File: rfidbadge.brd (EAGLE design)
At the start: 93.7 x 48.2 mm, 49 parts, among them Q1 BSS123, U1 ATMEGA328P_TQFP, U2 CLRC663, Y1 27.12 MHz

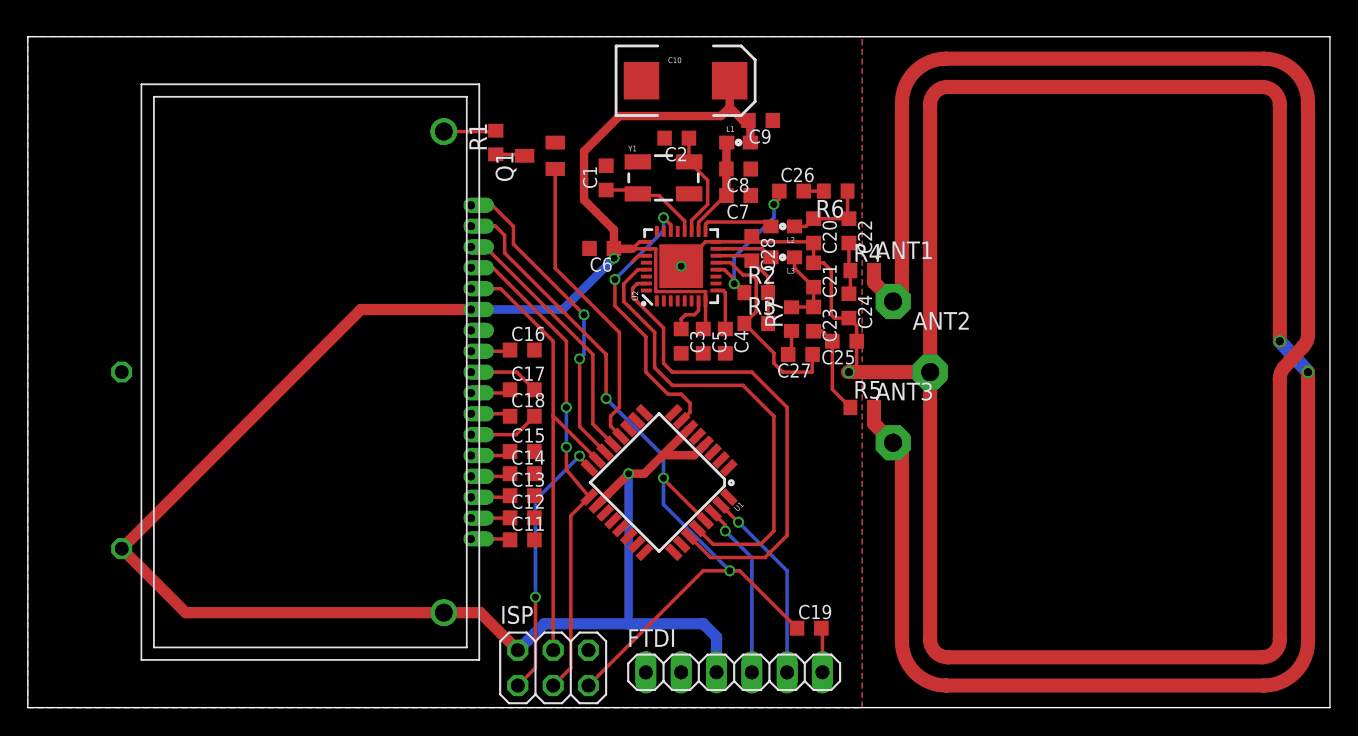
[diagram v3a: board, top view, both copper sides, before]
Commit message: Add switches, lanyard holes, rounded corners
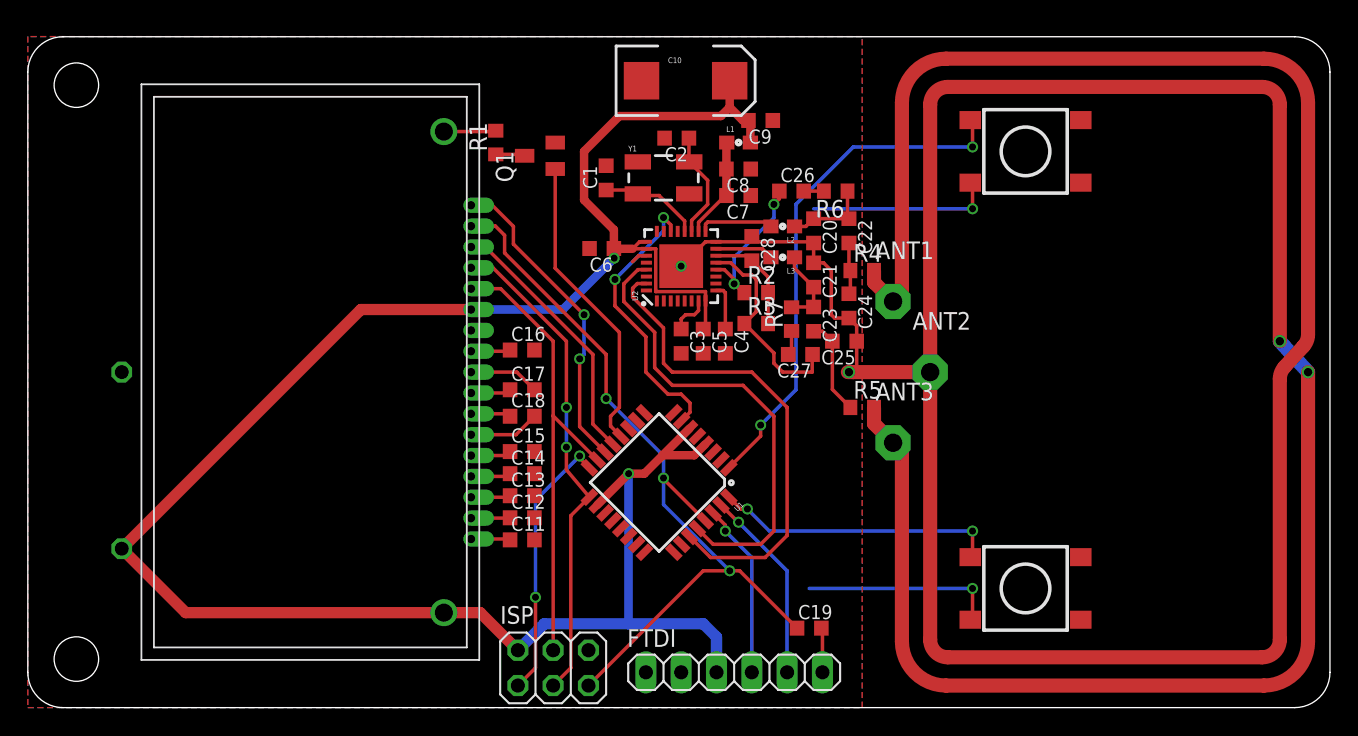
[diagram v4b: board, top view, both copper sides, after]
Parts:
- added S1, S2: SWITCH-MOMENTARY-2SMD-4, SparkFun-Electromechanical:TACTILE_SWITCH_TALL
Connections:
- new net PD2: S1.A2, U1.32
- new net PD3: S2.A2, U1.1
- net GND: now also S1.B2, S2.B2
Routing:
- net PD3: track 0.00 -> 37.5 mm, vias 0 -> 2
- net GND: track 298.4 -> 326.1 mm, vias 4 -> 6
- net PD2: track 0.00 -> 20.6 mm, vias 0 -> 2
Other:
- outline, holes or cut-outs redrawn
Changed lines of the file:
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@@
 <layer number="43" name="vRestrict" color="2" fill="10" visible="yes" active="yes"/>
 <layer number="44" name="Drills" color="7" fill="1" visible="no" active="yes"/>
-<layer number="45" name="Holes" color="7" fill="1" visible="no" active="yes"/>
+<layer number="45" name="Holes" color="7" fill="1" visible="yes" active="yes"/>
 <layer number="46" name="Milling" color="3" fill="1" visible="no" active="yes"/>
 <layer number="47" name="Measures" color="7" fill="1" visible="no" active="yes"/>
@@
 <board>
 <plain>
-<wire x1="0" y1="0" x2="93.65" y2="0" width="0" layer="20"/>
-<wire x1="93.65" y1="0" x2="93.65" y2="48.25" width="0" layer="20"/>
-<wire x1="93.65" y1="48.25" x2="0" y2="48.25" width="0" layer="20"/>
-<wire x1="0" y1="48.25" x2="0" y2="0" width="0" layer="20"/>
+<wire x1="91.11" y1="48.25" x2="2.54" y2="48.25" width="0" layer="20"/>
+<wire x1="2.54" y1="48.25" x2="0" y2="45.71" width="0" layer="20" curve="90"/>
+<wire x1="0" y1="45.71" x2="0" y2="2.54" width="0" layer="20"/>
+<wire x1="0" y1="2.54" x2="2.54" y2="0" width="0" layer="20" curve="90"/>
+<wire x1="2.54" y1="0" x2="91.11" y2="0" width="0" layer="20"/>
+<wire x1="91.11" y1="0" x2="93.65" y2="2.54" width="0" layer="20" curve="90"/>
+<wire x1="93.65" y1="2.54" x2="93.65" y2="45.71" width="0" layer="20"/>
+<wire x1="93.65" y1="45.71" x2="91.11" y2="48.25" width="0" layer="20" curve="90"/>
+<hole x="3.4925" y="3.4925" drill="3.2"/>
+<hole x="3.4925" y="44.7675" drill="3.2"/>
 </plain>
 <attributes>
@@
 <attribute name="PROD_ID" value="36-2479-ND" x="30.48" y="24.13" size="1.778" layer="28" rot="MR0" display="off"/>
 </element>
+<element name="S1" library="SparkFun-Electromechanical" package="TACTILE_SWITCH_TALL" value="SWITCH-MOMENTARY-2SMD-4" x="71.755" y="8.5725" rot="R180">
+<attribute name="PROD_ID" value="SWCH-11966" x="71.755" y="8.5725" size="1.778" layer="27" rot="R180" display="off"/>
+</element>
+<element name="S2" library="SparkFun-Electromechanical" package="TACTILE_SWITCH_TALL" value="SWITCH-MOMENTARY-2SMD-4" x="71.755" y="40.005" rot="R180">
+<attribute name="PROD_ID" value="SWCH-11966" x="71.755" y="40.005" size="1.778" layer="27" rot="R180" display="off"/>
+</element>
 </elements>
 <signals>
@@
 <wire x1="44.49" y1="32.5" x2="43.93" y2="32.5" width="0.254" layer="1"/>
 <wire x1="43.93" y1="32.5" x2="43.4975" y2="32.0675" width="0.254" layer="1"/>
-<wire x1="43.4975" y1="32.0675" x2="40.4" y2="33.02" width="0" layer="19" extent="1-16"/>
+<contactref element="S1" pad="B2"/>
+<contactref element="S2" pad="B2"/>
+<wire x1="67.78" y1="6.3225" x2="67.945" y2="6.3225" width="0.254" layer="1"/>
+<wire x1="67.945" y1="6.3225" x2="67.945" y2="8.5725" width="0.254" layer="1"/>
+<via x="67.945" y="8.5725" extent="1-16" drill="0.5"/>
+<wire x1="67.945" y1="8.5725" x2="56.1975" y2="8.5725" width="0.254" layer="16"/>
+<wire x1="67.78" y1="37.755" x2="67.945" y2="37.755" width="0.254" layer="1"/>
+<wire x1="67.945" y1="37.755" x2="67.945" y2="35.8775" width="0.254" layer="1"/>
+<via x="67.945" y="35.8775" extent="1-16" drill="0.5"/>
+<wire x1="67.945" y1="35.8775" x2="56.515" y2="35.8775" width="0.254" layer="16"/>
+<wire x1="48.15498125" y1="19.51066875" x2="48.5775" y2="25.4775" width="0" layer="19" extent="1-1"/>
 </signal>
 <signal name="EXTCLK">
@@
 <wire x1="46.99" y1="27.94" x2="46.99" y2="27.2275" width="0.254" layer="1"/>
 </signal>
+<signal name="PD2">
+<contactref element="U1" pad="32"/>
+<contactref element="S1" pad="A2"/>
+<wire x1="67.78" y1="10.8225" x2="67.945" y2="10.8225" width="0.254" layer="1"/>
+<wire x1="67.945" y1="10.8225" x2="67.945" y2="12.7" width="0.254" layer="1"/>
+<via x="67.945" y="12.7" extent="1-16" drill="0.5"/>
+<wire x1="67.945" y1="12.7" x2="53.34" y2="12.7" width="0.254" layer="16"/>
+<wire x1="53.34" y1="12.7" x2="51.7525" y2="14.2875" width="0.254" layer="16"/>
+<via x="51.7525" y="14.2875" extent="1-16" drill="0.5"/>
+<wire x1="51.7525" y1="14.2875" x2="51.267296875" y2="14.2875" width="0.254" layer="1"/>
+<wire x1="51.267296875" y1="14.2875" x2="50.417725" y2="15.137071875" width="0.254" layer="1"/>
+</signal>
+<signal name="PD3">
+<contactref element="U1" pad="1"/>
+<contactref element="S2" pad="A2"/>
+<wire x1="67.78" y1="42.255" x2="67.945" y2="42.255" width="0.254" layer="1"/>
+<wire x1="67.945" y1="42.255" x2="67.945" y2="40.3225" width="0.254" layer="1"/>
+<via x="67.945" y="40.3225" extent="1-16" drill="0.5"/>
+<wire x1="67.945" y1="40.3225" x2="59.3725" y2="40.3225" width="0.254" layer="16"/>
+<wire x1="59.3725" y1="40.3225" x2="55.245" y2="36.195" width="0.254" layer="16"/>
+<wire x1="55.245" y1="36.195" x2="55.245" y2="22.86" width="0.254" layer="16"/>
+<wire x1="55.245" y1="22.86" x2="52.705" y2="20.32" width="0.254" layer="16"/>
+<via x="52.705" y="20.32" extent="1-16" drill="0.5"/>
+<wire x1="52.705" y1="20.32" x2="52.705" y2="19.5352" width="0.254" layer="1"/>
+<wire x1="52.705" y1="19.5352" x2="50.417725" y2="17.247925" width="0.254" layer="1"/>
+</signal>
 </signals>

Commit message: I like fat traces and I cannot lie
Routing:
- net GND: track 326.1 -> 325.5 mm

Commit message: Added some test pads
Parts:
- added TP1, TP2, TP3, TP4, TP5, TP6: TPTP06R, testpad:TP06R
- moved C3 2.25 mm to (48.6, 24.8), turned to 0 degrees
- moved C4 2.25 mm to (51.8, 24.8), turned to 0 degrees
- moved C5 1.14 mm to (49.5, 27.0)
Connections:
- new net N$12: TP3.TP, U2.3
- new net N$13: TP4.TP, U2.4
- new net N$14: TP5.TP, U2.5
- new net N$15: TP6.TP, U2.6
- new net N$5: TP1.TP, U2.1
- new net N$6: TP2.TP, U2.2
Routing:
- net N$6: track 0.00 -> 3.17 mm
- net N$13: track 0.00 -> 3.06 mm
- net N$15: track 0.00 -> 2.95 mm
- net N$10: track 3.36 -> 6.11 mm
- net N$5: track 0.00 -> 2.27 mm
- net N$12: track 0.00 -> 2.16 mm
- net N$14: track 0.00 -> 2.05 mm
- net N$11: track 2.91 -> 4.71 mm

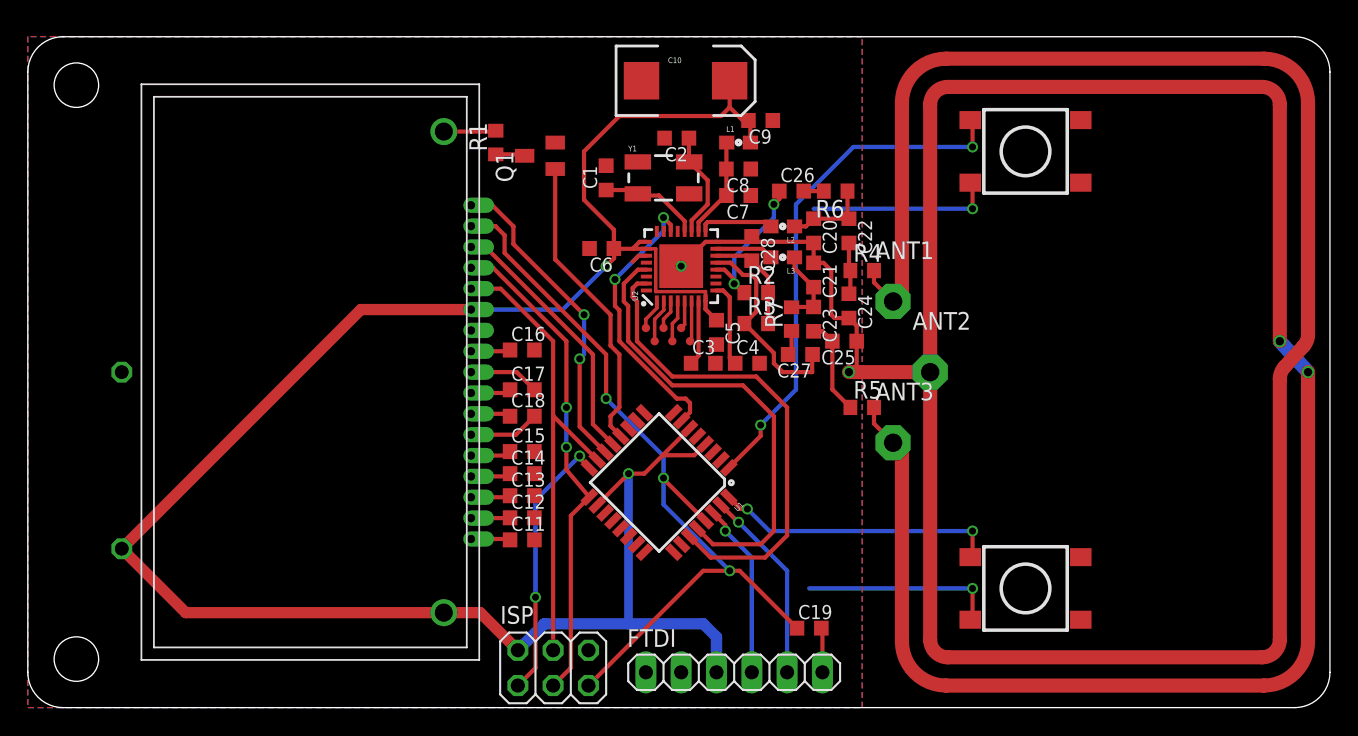
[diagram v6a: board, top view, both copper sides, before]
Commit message: Fix ground loops and islands
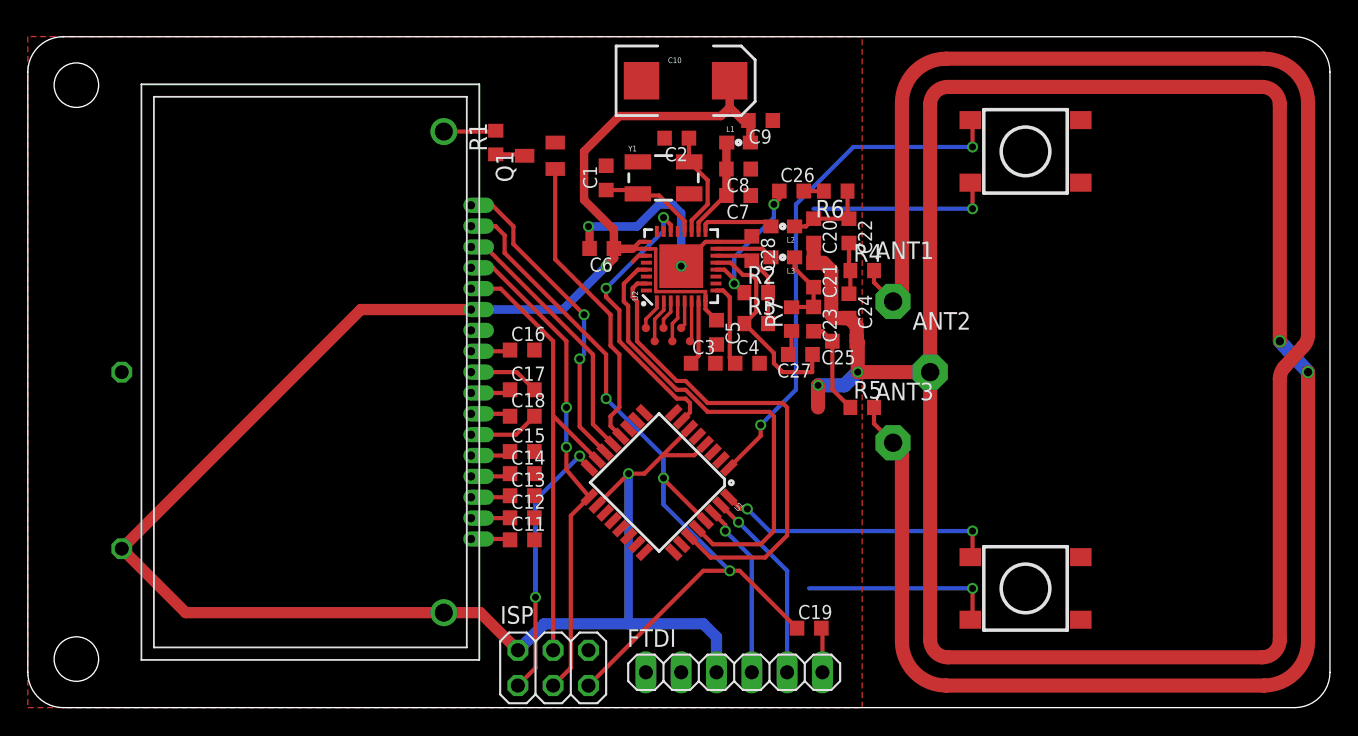
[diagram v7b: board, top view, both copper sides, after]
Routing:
- net GND: track 325.5 -> 338.5 mm, vias 6 -> 8
- net EXTCLK: track 20.1 -> 20.6 mm
- removed copper zone on layer 16, net GND

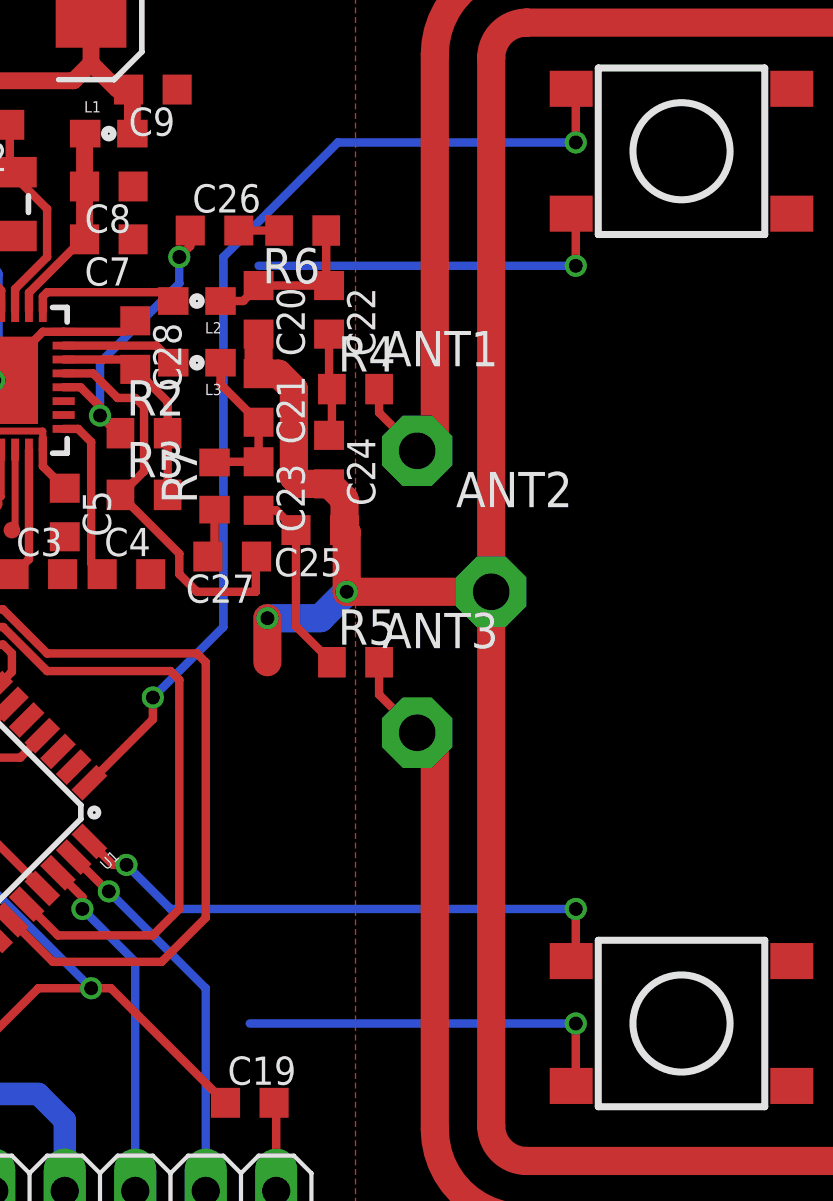
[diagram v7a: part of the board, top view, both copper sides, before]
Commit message: Fix button grounds
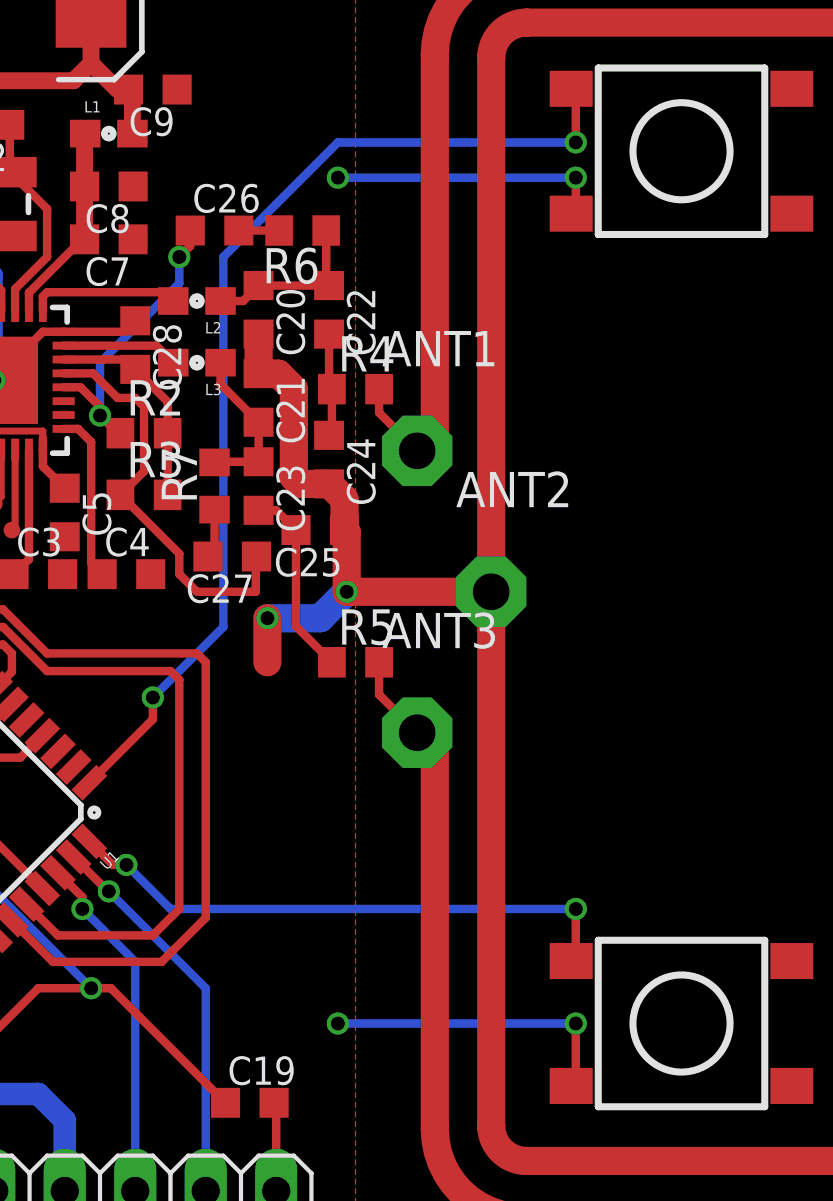
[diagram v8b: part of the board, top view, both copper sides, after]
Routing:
- net GND: track 338.5 -> 331.9 mm, vias 8 -> 10
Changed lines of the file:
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@@
 <wire x1="67.945" y1="6.3225" x2="67.945" y2="8.5725" width="0.3048" layer="1"/>
 <via x="67.945" y="8.5725" extent="1-16" drill="0.5"/>
-<wire x1="67.945" y1="8.5725" x2="56.1975" y2="8.5725" width="0.3048" layer="16"/>
 <wire x1="67.78" y1="37.755" x2="67.945" y2="37.755" width="0.3048" layer="1"/>
-<wire x1="67.945" y1="37.755" x2="67.945" y2="35.8775" width="0.3048" layer="1"/>
-<via x="67.945" y="35.8775" extent="1-16" drill="0.5"/>
-<wire x1="67.945" y1="35.8775" x2="56.515" y2="35.8775" width="0.3048" layer="16"/>
 <wire x1="62.865" y1="19.05" x2="62.23" y2="19.05" width="1.016" layer="1"/>
 <wire x1="60.8575" y1="31.4325" x2="60.8575" y2="30.5825" width="0.3048" layer="1"/>
@@
 <wire x1="59.69" y1="26.275" x2="59.69" y2="24.13" width="1.016" layer="1"/>
 <wire x1="59.6125" y1="26.3525" x2="59.6125" y2="27.46" width="1.016" layer="1"/>
-<wire x1="56.43" y1="33.5" x2="56.515" y2="35.8775" width="0" layer="19" extent="1-16"/>
-<wire x1="67.78" y1="6.3225" x2="66.167" y2="3.6195" width="0" layer="19" extent="1-1"/>
-<wire x1="36.435" y1="12.065" x2="42.650015625" y2="12.874328125" width="0" layer="19" extent="1-1"/>
+<wire x1="67.945" y1="37.755" x2="67.945" y2="39.0525" width="0.3048" layer="1"/>
+<via x="67.945" y="39.0525" extent="1-16" drill="0.5"/>
+<wire x1="67.945" y1="39.0525" x2="59.3725" y2="39.0525" width="0.3048" layer="16"/>
+<via x="59.3725" y="39.0525" extent="1-16" drill="0.5"/>
+<wire x1="67.945" y1="8.5725" x2="59.3725" y2="8.5725" width="0.3048" layer="16"/>
+<via x="59.3725" y="8.5725" extent="1-16" drill="0.5"/>
+<wire x1="42.650015625" y1="12.874328125" x2="36.435" y2="12.065" width="0" layer="19" extent="1-1"/>
 </signal>
 <signal name="EXTCLK">
